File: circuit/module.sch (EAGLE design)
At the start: 12 parts, among them IC1 4050

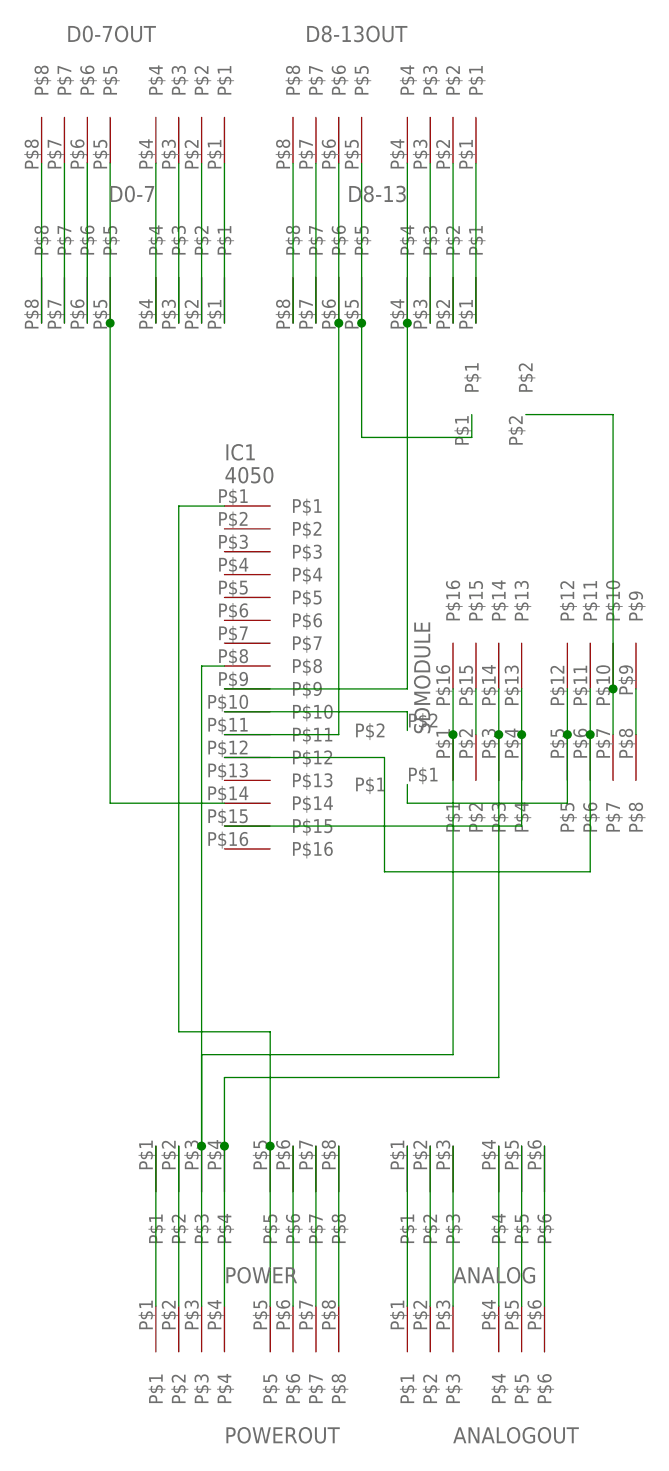
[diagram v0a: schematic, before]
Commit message: Move 4050 to the right side of the SD module. Remove male-female pin couples, instead use a single group of pins.
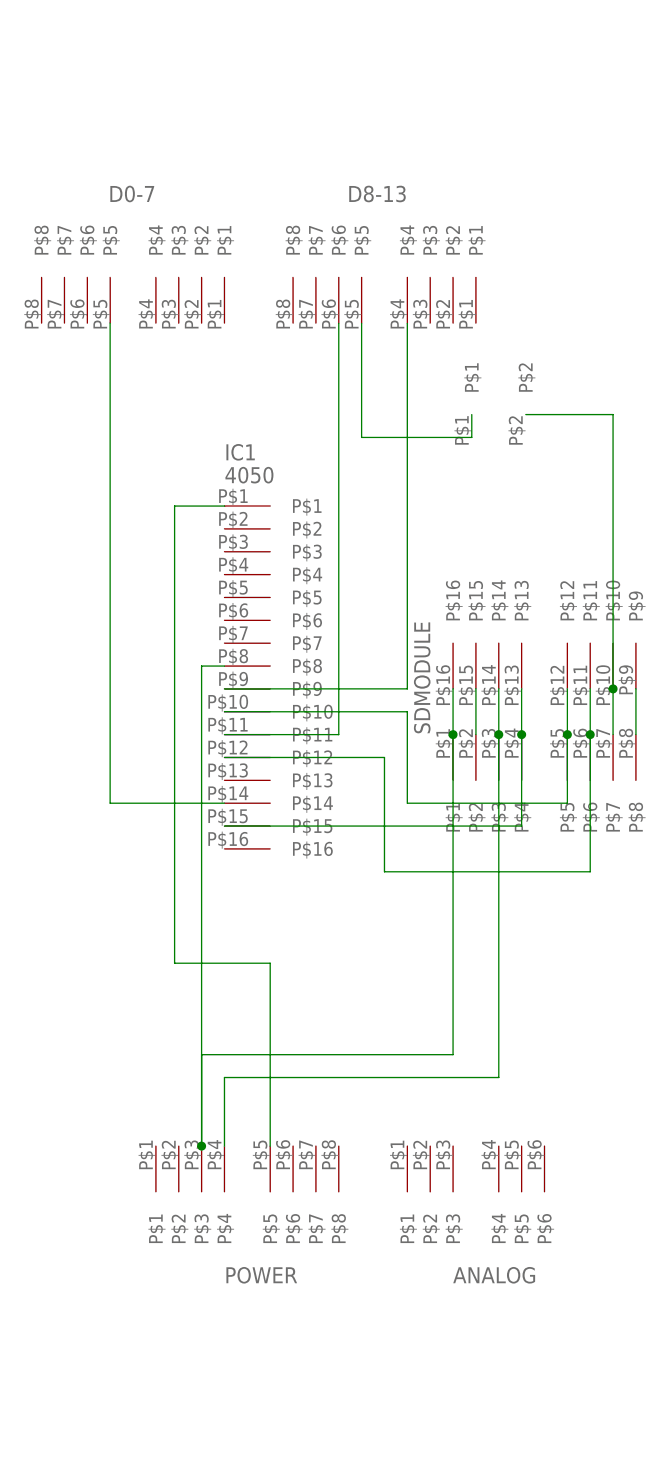
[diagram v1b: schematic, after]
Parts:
- removed ANALOGOUT: PINPLUG6PINPLUG6, simple-parts:PINPLUG6PINPLUG6
- removed D0-7OUT, D8-13OUT, POWEROUT: PINPLUG8PINPLUG8, simple-parts:PINPLUG8PINPLUG8
- removed U$2: SHORTSHORT5, simple-parts:SHORTSHORT5
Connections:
- removed net N$10: D8-13.P$7, D8-13OUT.P$7
- removed net N$14: D8-13.P$3, D8-13OUT.P$3
- removed net N$15: D8-13.P$2, D8-13OUT.P$2
- removed net N$16: D8-13.P$1, D8-13OUT.P$1
- removed net N$17: POWER.P$1, POWEROUT.P$1
- removed net N$18: POWER.P$2, POWEROUT.P$2
- removed net N$2: D0-7.P$7, D0-7OUT.P$7
- removed net N$21: IC1.P$10, U$2.P$2
- removed net N$23: POWER.P$6, POWEROUT.P$6
- removed net N$24: POWER.P$7, POWEROUT.P$7
- removed net N$25: POWER.P$8, POWEROUT.P$8
- removed net N$26: ANALOG.P$1, ANALOGOUT.P$1
- removed net N$27: ANALOG.P$2, ANALOGOUT.P$2
- removed net N$28: ANALOG.P$3, ANALOGOUT.P$3
- removed net N$29: ANALOG.P$4, ANALOGOUT.P$4
- removed net N$3: D0-7.P$6, D0-7OUT.P$6
- removed net N$30: ANALOG.P$5, ANALOGOUT.P$5
- removed net N$31: ANALOG.P$6, ANALOGOUT.P$6
- removed net N$40: IC1.P$1, POWER.P$5, POWEROUT.P$5
- removed net N$5: D0-7.P$4, D0-7OUT.P$4
- removed net N$6: D0-7.P$3, D0-7OUT.P$3
- removed net N$7: D0-7.P$2, D0-7OUT.P$2
- removed net N$8: D0-7.P$1, D0-7OUT.P$1
- removed net N$9: D8-13.P$8, D8-13OUT.P$8
- net N$1: now also IC1.P$1, POWER.P$5; no longer D0-7.P$8, D0-7OUT.P$8
- net N$13: no longer D8-13OUT.P$4
- net N$20: no longer POWEROUT.P$3
- net N$22: no longer D8-13OUT.P$5
- net N$33: now also IC1.P$10; no longer U$2.P$1
- net N$34: no longer D8-13OUT.P$6
- net N$39: no longer POWEROUT.P$4
- net N$4: no longer D0-7OUT.P$5
